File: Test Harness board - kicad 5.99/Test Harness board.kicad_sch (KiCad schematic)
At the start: 5 parts, among them U1 TCA9548APWR

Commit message: Starting the test harness board
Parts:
- gave numbers to parts that had none: 1
- renumbered J_PWR to J_PWR1
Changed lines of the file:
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@@
   (symbol (lib_id "power:+5V") (at 36.83 29.21 0) (unit 1)
     (in_bom yes) (on_board yes)
-    (property "Reference" "#PWR?" (id 0) (at 36.83 33.02 0)
+    (property "Reference" "#PWR0103" (id 0) (at 36.83 33.02 0)
       (effects (font (size 1.27 1.27)) hide)
     )
@@
   (symbol (lib_id "power:+5V") (at 39.37 107.95 0) (unit 1)
     (in_bom yes) (on_board yes)
-    (property "Reference" "#PWR?" (id 0) (at 39.37 111.76 0)
+    (property "Reference" "#PWR0104" (id 0) (at 39.37 111.76 0)
       (effects (font (size 1.27 1.27)) hide)
     )
@@
   (symbol (lib_id "power:+5V") (at 243.84 40.64 0) (unit 1)
     (in_bom yes) (on_board yes)
-    (property "Reference" "#PWR?" (id 0) (at 243.84 44.45 0)
+    (property "Reference" "#PWR0106" (id 0) (at 243.84 44.45 0)
       (effects (font (size 1.27 1.27)) hide)
     )
@@
   (symbol (lib_id "power:GND") (at 39.37 88.9 0) (unit 1)
     (in_bom yes) (on_board yes)
-    (property "Reference" "#PWR?" (id 0) (at 39.37 95.25 0)
+    (property "Reference" "#PWR0105" (id 0) (at 39.37 95.25 0)
       (effects (font (size 1.27 1.27)) hide)
     )
@@
   (symbol (lib_id "power:GND") (at 39.37 163.83 0) (unit 1)
     (in_bom yes) (on_board yes)
-    (property "Reference" "#PWR?" (id 0) (at 39.37 170.18 0)
+    (property "Reference" "#PWR0102" (id 0) (at 39.37 170.18 0)
       (effects (font (size 1.27 1.27)) hide)
     )
@@
   (symbol (lib_id "power:GND") (at 259.08 54.61 0) (unit 1)
     (in_bom yes) (on_board yes)
-    (property "Reference" "#PWR?" (id 0) (at 259.08 60.96 0)
+    (property "Reference" "#PWR0101" (id 0) (at 259.08 60.96 0)
       (effects (font (size 1.27 1.27)) hide)
     )
@@
   (symbol (lib_id "Connector:Screw_Terminal_01x02") (at 256.54 22.86 90) (unit 1)
     (in_bom yes) (on_board yes)
-    (property "Reference" "J_PWR" (id 0) (at 261.62 22.86 90)
+    (property "Reference" "J_PWR1" (id 0) (at 261.62 22.86 90)
       (effects (font (size 1.27 1.27)) (justify right))
     )
@@
   (symbol (lib_id "MCU_Module:Arduino_Nano_Every") (at 39.37 57.15 0) (unit 1)
     (in_bom yes) (on_board yes)
-    (property "Reference" "A?" (id 0) (at 27.94 82.55 0))
+    (property "Reference" "A1" (id 0) (at 27.94 82.55 0))
     (property "Value" "Arduino_Nano_Every" (id 1) (at 27.94 85.09 0))
     (property "Footprint" "Module:Arduino_Nano" (id 2) (at 39.37 57.15 0)
@@
   )
   (symbol_instances
+    (path "/ca267f34-0525-44e9-a759-8a1dac3c575e"
+      (reference "#PWR0101") (unit 1)
+    )
+    (path "/e27464af-bff2-488d-b48b-cce80ac3de1f"
+      (reference "#PWR0102") (unit 1)
+    )
+    (path "/b99f28a2-8a5b-4dd5-9604-3a04d2b648dd"
+      (reference "#PWR0103") (unit 1)
+    )
     (path "/3842a3e7-2ee9-45a9-b4bd-4fdd33de3048"
-      (reference "#PWR?") (unit 1)
+      (reference "#PWR0104") (unit 1)
     )
     (path "/50a545cf-364f-40a3-94b3-e9316e26c018"
-      (reference "#PWR?") (unit 1)
-    )
-    (path "/b99f28a2-8a5b-4dd5-9604-3a04d2b648dd"
-      (reference "#PWR?") (unit 1)
-    )
-    (path "/ca267f34-0525-44e9-a759-8a1dac3c575e"
-      (reference "#PWR?") (unit 1)
+      (reference "#PWR0105") (unit 1)
     )
     (path "/ddff20db-f520-4fc7-8f8e-498c172721dd"
-      (reference "#PWR?") (unit 1)
-    )
-    (path "/e27464af-bff2-488d-b48b-cce80ac3de1f"
-      (reference "#PWR?") (unit 1)
+      (reference "#PWR0106") (unit 1)
     )
     (path "/8863af52-81ac-4750-8f8e-00c63e3b5ab0"
-      (reference "A?") (unit 1)
+      (reference "A1") (unit 1)
     )
     (path "/5b521b6c-92ed-4745-882c-b3c25500e203"
@@
     )
     (path "/195cf52e-98e4-48b0-8f16-66fa3836a118"
-      (reference "J_PWR") (unit 1)
+      (reference "J_PWR1") (unit 1)
     )
     (path "/d96f55c9-d554-4e7f-a64b-7e70f4ccef89"
       (reference "U1") (unit 1)
     )
-    (path "/0bb7ffcb-56f8-4343-bb38-9a762c1c79b6/035fa1ab-3470-4dc0-a3a1-44be9fe0bb2a"
-      (reference "J_LEFT?") (unit 1)
-    )
-    (path "/0bb7ffcb-56f8-4343-bb38-9a762c1c79b6/c957d363-432c-40f3-97c7-175e7b1893a0"
-      (reference "J_LEFT?") (unit 2)
-    )
-    (path "/0bb7ffcb-56f8-4343-bb38-9a762c1c79b6/40b92a5c-b0ca-416a-9882-87140c7f57bf"
-      (reference "J_LEFT?") (unit 3)
-    )
-  )
+    (path "/0bb7ffcb-56f8-4343-bb38-9a762c1c79b6/1c22360a-19d9-48eb-9954-a9e109401ce7"
+      (reference "#PWR0107") (unit 1)
+    )
+    (path "/0bb7ffcb-56f8-4343-bb38-9a762c1c79b6/1f9d4fb8-893a-4921-97a5-a950fbddb477"
+      (reference "#PWR0108") (unit 1)
+    )
+    (path "/0bb7ffcb-56f8-4343-bb38-9a762c1c79b6/7f29476d-3e32-4358-bffa-e93138449a4c"
+      (reference "#PWR0109") (unit 1)
+    )
+    (path "/0bb7ffcb-56f8-4343-bb38-9a762c1c79b6/0d6b8021-34fc-440f-aa31-d30da1a6c75d"
+      (reference "#PWR0110") (unit 1)
+    )
+    (path "/0bb7ffcb-56f8-4343-bb38-9a762c1c79b6/38a3fe33-52b1-461d-bd39-3dd49715b7e0"
+      (reference "#PWR0111") (unit 1)
+    )
+    (path "/0bb7ffcb-56f8-4343-bb38-9a762c1c79b6/47d2ca3d-ab3d-4c50-a08f-70a2acca64ee"
+      (reference "#PWR0112") (unit 1)
+    )
+    (path "/0bb7ffcb-56f8-4343-bb38-9a762c1c79b6/65a70845-3919-4145-86bc-bd1c99f87fa8"
+      (reference "#PWR0113") (unit 1)
+    )
+    (path "/0bb7ffcb-56f8-4343-bb38-9a762c1c79b6/324bc777-75f3-4f44-a253-12e791a08e75"
+      (reference "#PWR0114") (unit 1)
+    )
+    (path "/0bb7ffcb-56f8-4343-bb38-9a762c1c79b6/3aab7c33-2daa-441f-b386-264be68eaa18"
+      (reference "#PWR0115") (unit 1)
+    )
+    (path "/0bb7ffcb-56f8-4343-bb38-9a762c1c79b6/90a273c5-38e4-4e4d-9eae-45908bacb69c"
+      (reference "#PWR0116") (unit 1)
+    )
+    (path "/0bb7ffcb-56f8-4343-bb38-9a762c1c79b6/23a077b5-f60e-452c-8354-84b5e0bdaf78"
+      (reference "#PWR0117") (unit 1)
+    )
+    (path "/0bb7ffcb-56f8-4343-bb38-9a762c1c79b6/3fbbea5d-b722-4687-92b2-710f9af29c96"
+      (reference "#PWR0118") (unit 1)
+    )
+    (path "/0bb7ffcb-56f8-4343-bb38-9a762c1c79b6/4a5a9a62-bf63-495a-917b-0eeda80f6bf9"
+      (reference "#PWR0119") (unit 1)
+    )
+    (path "/0bb7ffcb-56f8-4343-bb38-9a762c1c79b6/41a42bba-20c0-4bd4-a31c-91561f2501b8"
+      (reference "#PWR0120") (unit 1)
+    )
+    (path "/0bb7ffcb-56f8-4343-bb38-9a762c1c79b6/e8185962-55a2-408d-9346-2ea696f130bc"
+      (reference "#PWR0121") (unit 1)
+    )
+    (path "/0bb7ffcb-56f8-4343-bb38-9a762c1c79b6/5024b5f7-8974-4589-abb9-266207a27b9a"
+      (reference "#PWR0122") (unit 1)
+    )
+    (path "/0bb7ffcb-56f8-4343-bb38-9a762c1c79b6/75837aa1-994c-45ff-8f9e-2b5f305d9a47"
+      (reference "C1") (unit 1)
+    )
+    (path "/0bb7ffcb-56f8-4343-bb38-9a762c1c79b6/e89bce97-0629-4a58-9152-736ad89f0a50"
+      (reference "C1_1") (unit 1)
+    )
+    (path "/0bb7ffcb-56f8-4343-bb38-9a762c1c79b6/3f892dc3-18d8-4759-b7f2-146ee45fedde"
+      (reference "C1_2") (unit 1)
+    )
+    (path "/0bb7ffcb-56f8-4343-bb38-9a762c1c79b6/60f4683b-8d79-4620-833b-36c38686da9c"
+      (reference "D_L0") (unit 1)
+    )
+    (path "/0bb7ffcb-56f8-4343-bb38-9a762c1c79b6/f501a700-bd55-4a8f-8b4d-49cf8edfe51b"
+      (reference "D_L1") (unit 1)
+    )
+    (path "/0bb7ffcb-56f8-4343-bb38-9a762c1c79b6/d15d5cb4-6e55-48c2-885f-054fdd19320f"
+      (reference "D_L2") (unit 1)
+    )
+    (path "/0bb7ffcb-56f8-4343-bb38-9a762c1c79b6/2a0c4d64-2a44-4242-bc97-4b1c49405e38"
+      (reference "D_L3") (unit 1)
+    )
+    (path "/0bb7ffcb-56f8-4343-bb38-9a762c1c79b6/9db014fb-b466-4f04-a5c6-c00e546fa8d3"
+      (reference "D_L4") (unit 1)
+    )
+    (path "/0bb7ffcb-56f8-4343-bb38-9a762c1c79b6/76bf7d96-c104-4774-b79f-0c8ade49b6c2"
+      (reference "D_L5") (unit 1)
+    )
+    (path "/0bb7ffcb-56f8-4343-bb38-9a762c1c79b6/58f98de2-aa45-45d6-89ed-54f7e6ee9fc1"
+      (reference "D_L6") (unit 1)
+    )
+    (path "/0bb7ffcb-56f8-4343-bb38-9a762c1c79b6/8dede177-051d-4358-a681-c4b2484827df"
+      (reference "D_L7") (unit 1)
+    )
+    (path "/0bb7ffcb-56f8-4343-bb38-9a762c1c79b6/7bf95e30-2dec-43c6-8bb6-175acb91e138"
+      (reference "D_L8") (unit 1)
+    )
+    (path "/0bb7ffcb-56f8-4343-bb38-9a762c1c79b6/b268e150-054f-4582-9c2a-f3f0b91fc0c7"
+      (reference "D_L9") (unit 1)
+    )
+    (path "/0bb7ffcb-56f8-4343-bb38-9a762c1c79b6/7cecfc91-266e-40fb-9047-5d0023843f71"
+      (reference "D_L10") (unit 1)
+    )
+    (path "/0bb7ffcb-56f8-4343-bb38-9a762c1c79b6/a2d5058e-e5f9-46ea-b6a4-90ce25e43d7c"
+      (reference "D_L11") (unit 1)
+    )
+    (path "/0bb7ffcb-56f8-4343-bb38-9a762c1c79b6/75f83043-6ec4-4615-b855-48acda957f2e"
+      (reference "D_L12") (unit 1)
+    )
+    (path "/0bb7ffcb-56f8-4343-bb38-9a762c1c79b6/5a07387c-8a2e-4811-8fd4-47e0922ecf86"
+      (reference "D_L13") (unit 1)
+    )
+    (path "/0bb7ffcb-56f8-4343-bb38-9a762c1c79b6/fc84862e-fe2b-4167-b057-0311fcf1630a"
+      (reference "D_L14") (unit 1)
+    )
+    (path "/0bb7ffcb-56f8-4343-bb38-9a762c1c79b6/d5e080a4-99dd-4c99-bde3-c64ebd46b014"
+      (reference "D_L15") (unit 1)
+    )
+    (path "/0bb7ffcb-56f8-4343-bb38-9a762c1c79b6/90e12068-4e0f-41c5-b9d3-9a184834e4f8"
+      (reference "J_LEFT1") (unit 1)
+    )
+    (path "/0bb7ffcb-56f8-4343-bb38-9a762c1c79b6/55af7765-732c-42ea-99db-0424f12044b7"
+      (reference "RN1_1_1") (unit 1)
+    )
+    (path "/0bb7ffcb-56f8-4343-bb38-9a762c1c79b6/e03ffc21-1ee1-49de-aecd-49fc22e30cc3"
+      (reference "RN1_1_2") (unit 1)
+    )
+    (path "/0bb7ffcb-56f8-4343-bb38-9a762c1c79b6/8bc9344e-b791-4821-8e1a-c674834b8d75"
+      (reference "RN1_2_1") (unit 1)
+    )
+    (path "/0bb7ffcb-56f8-4343-bb38-9a762c1c79b6/2f0bd0e1-6019-487a-a204-7b22bb025e6a"
+      (reference "RN1_2_2") (unit 1)
+    )
+    (path "/0bb7ffcb-56f8-4343-bb38-9a762c1c79b6/06b61526-37e3-4c1a-887c-a56933b94d02"
+      (reference "UL1") (unit 1)
+    )
+    (path "/0bb7ffcb-56f8-4343-bb38-9a762c1c79b6/534e042c-7d84-4de1-89b0-47b98062c004"
+      (reference "UL1_1") (unit 1)
+    )
+    (path "/0bb7ffcb-56f8-4343-bb38-9a762c1c79b6/fed52245-9ddd-4426-a911-6f727e8d1f2b"
+      (reference "UL1_2") (unit 1)
+    )
+  )

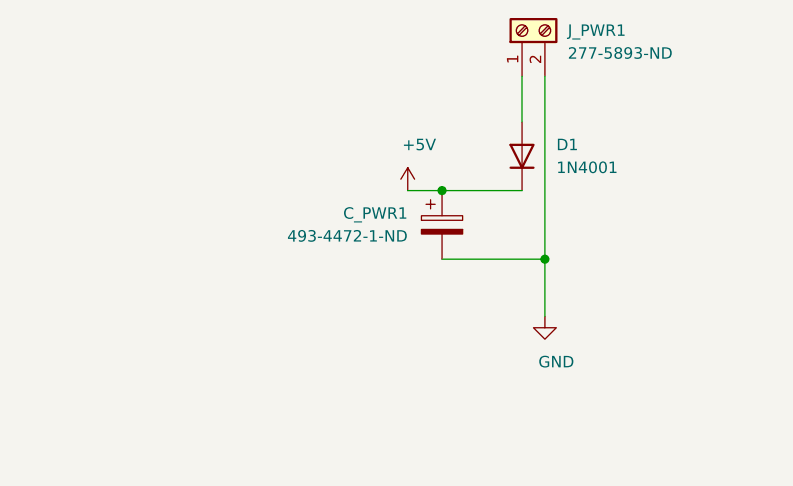
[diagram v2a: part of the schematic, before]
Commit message: restart on the test harness, made a more compact design (will need the 4 layers though)
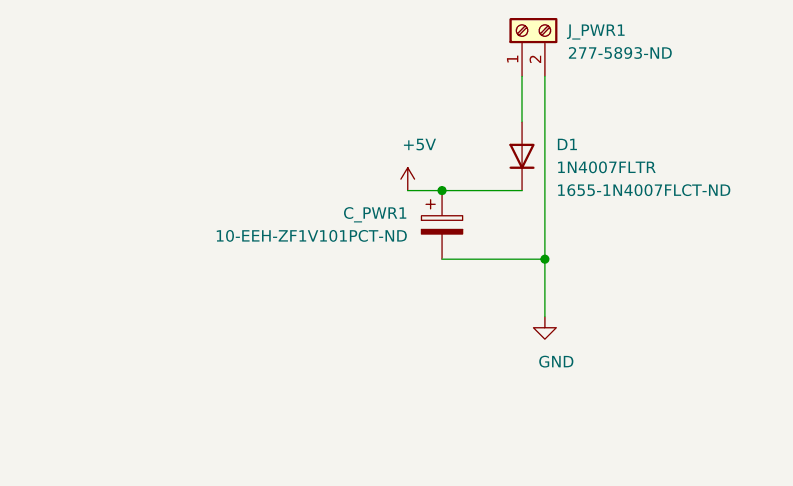
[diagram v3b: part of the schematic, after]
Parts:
- C_PWR1: footprint Capacitor_SMD:CP_Elec_18x22 -> Capacitor_SMD:CP_Elec_8x10; Digikey 493-4472-1-ND -> 10-EEH-ZF1V101PCT-ND
- D1: value 1N4001 -> 1N4007FLTR; footprint Diode_THT:D_DO-41_SOD81_P10.16mm_Horizontal -> Diode_SMD:D_SOD-123F; symbol Diode:1N4001 -> Diode:1N4007; Digikey (none) -> 1655-1N4007FLCT-ND
